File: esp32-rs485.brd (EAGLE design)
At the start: 160 x 100 mm, 24 parts, among them J1 GREEN-2P-3.5, U1 TEXAS_INSTRUMENTS_TPS54360DDA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, U2 MAX3485CSA

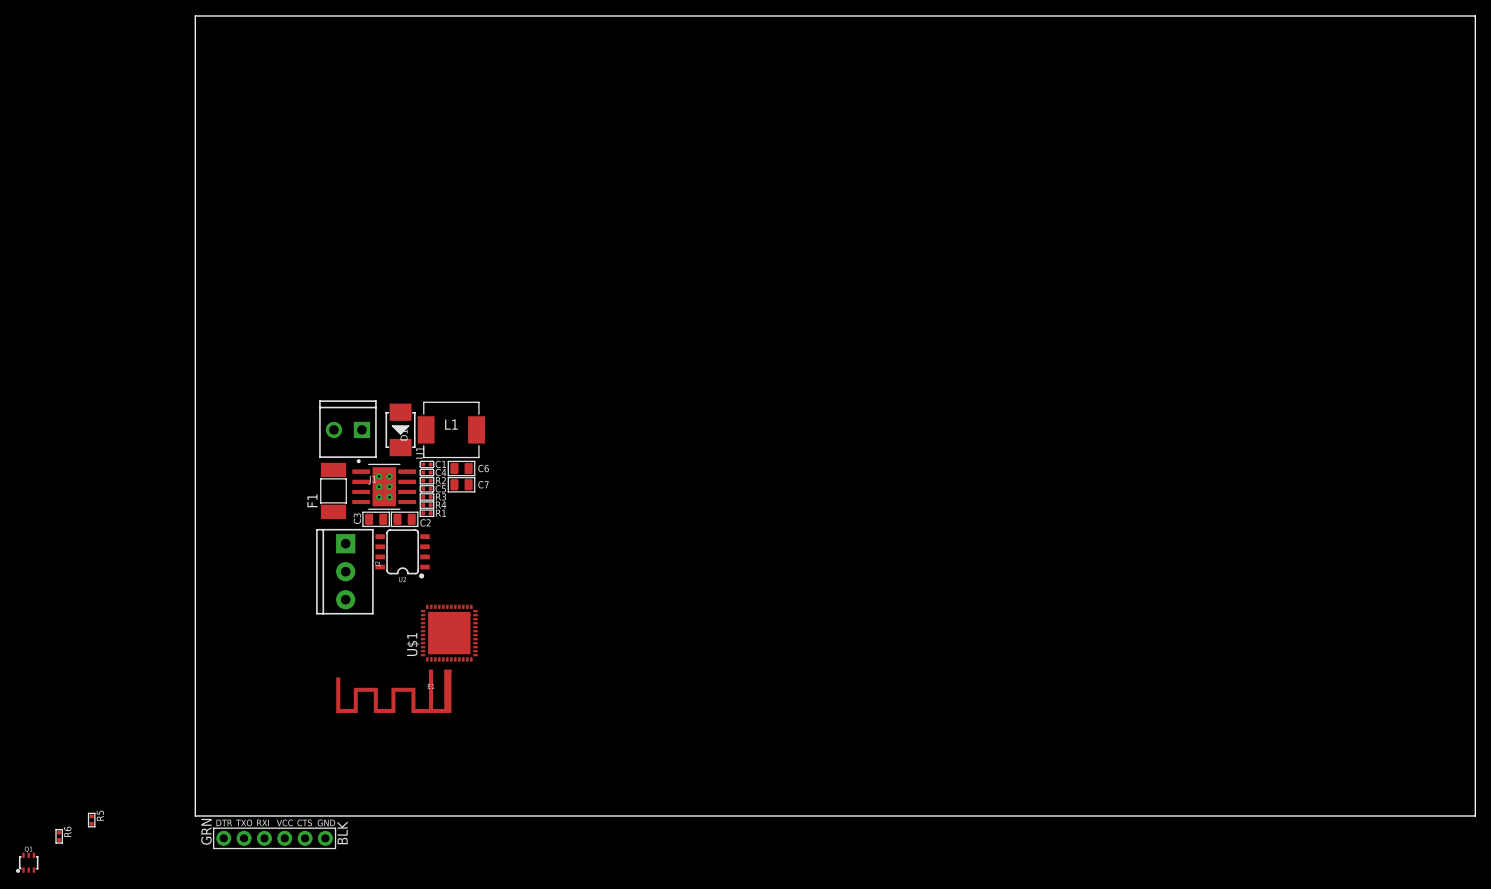
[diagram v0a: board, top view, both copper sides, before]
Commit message: Add MAX3485, CH340K and associated passives
Add MAX3485 TTL serial to RS-485 transceiver and associated passives.
Add CH340K USB to TTL serial chip and associated passives, ESP reset circuitry and PCB edge USB-C connector (must use 0.8mm PCB).
Complete PCB layout.
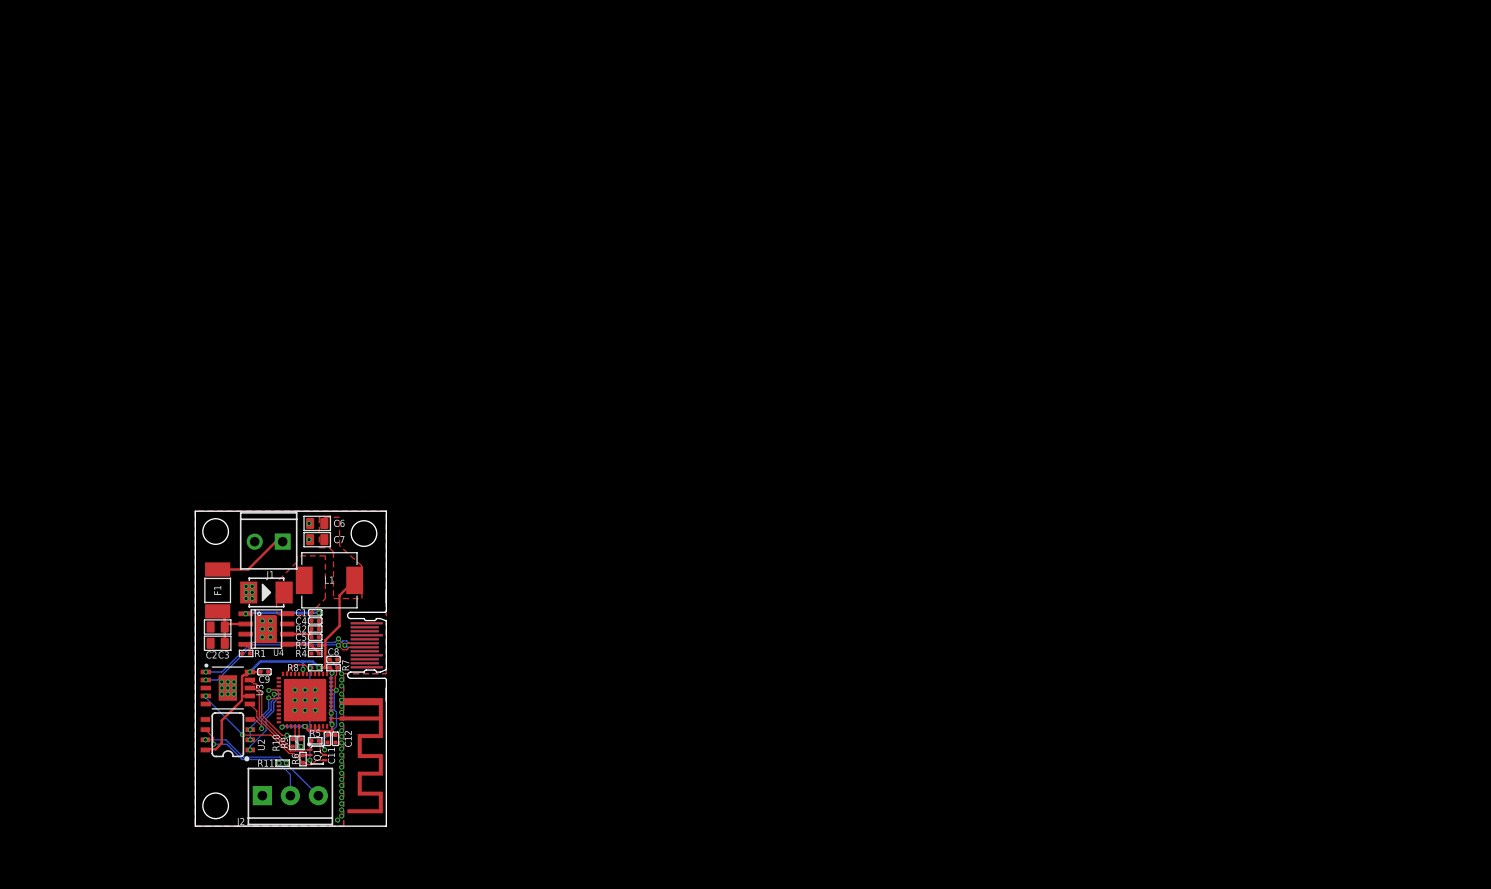
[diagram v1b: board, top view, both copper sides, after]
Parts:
- removed J3: (no value), SparkFun-Connectors:6_PIN_SERIAL_TARGET_SIDE_W_SILK
- removed U$1: ESP32-PICO-D4, ESP32-PICO-D4:QFN48
- added C11, C8, C9: 100nf, OPL_Capacitor:C0402
- added C12: 1UF 6.3V, OPL_Capacitor:C0402
- added R10, R9: 470R, OPL_Resistor:R0402
- added R11: 220R, OPL_Resistor:R0402
- added R7, R8: 10K 1/16W, OPL_Resistor:R0402
- added U$2: PCB_USB_C_2.0DS_2, USB_pcb_connectors:USB_TYPE_C_DS_2
- added U3: CH340K, CH340K:SOP100P600X180-11T230X320N
- added U4: TPS54360, we-power:SO08-PAD
- U1: value TEXAS_INSTRUMENTS_TPS54360DDARTEXAS_INSTRUMENTS_TPS54360DDAR_0_0 -> ESP32-PICO-D4; device Texas Instruments - TPS54360DDAR:TEXAS_INSTRUMENTS_TPS54360DDAR_0 -> ESP32-PICO-D4:QFN48
- moved Q1 38.5 mm to (15.2, 7.62), turned to 270 degrees
- moved J2 33.2 mm to (8.38, 2.54), turned to 0 degrees
- moved R6 32.0 mm to (13.5, 7.11), turned to 180 degrees
- moved U2 31.6 mm to (4.06, 10.2)
- moved R5 29.6 mm to (15.0, 9.40), turned to 90 degrees
- moved R1 28.6 mm to (6.35, 20.3), turned to 90 degrees
- moved U1 28.5 mm to (13.7, 14.5), turned to 180 degrees
- moved C2 27.0 mm to (2.79, 23.6), turned to 90 degrees
- moved D1 26.3 mm to (8.89, 27.9), turned to 0 degrees
- moved C3 25.2 mm to (2.79, 21.6)
- moved L1 24.2 mm to (16.8, 29.5)
- moved C1 23.2 mm to (15.0, 25.4)
- moved C4 23.2 mm to (15.0, 24.4)
- moved R3 23.2 mm to (15.0, 21.3)
- moved R4 23.2 mm to (15.0, 20.3), turned to 90 degrees
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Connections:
- removed net N$5: C2.2, C3.2, F1.1, U1.2
- removed net N$7: C5.2, R2.2, U1.6
- removed net VDD3P3_CPU: U$1.37
- removed net VDD3P3_RTC: U$1.19
- removed net VDDA_2: U$1.43
- removed net VDDA_3: U$1.46
- new net +24V: C2.2, C3.2, F1.1, U4.2
- new net DTR: Q1.4, R6.1, U3.4
- new net EN: C8.1, Q1.6, R7.1, U1.9
- new net GPIO0: Q1.3, R8.1, U1.23
- new net N$10: R10.1, U3.8
- new net N$11: R9.1, U3.9
- new net N$12: U$2.A6, U$2.B6, U3.2
- new net N$13: U$2.A7, U$2.B7, U3.1
- new net N$14: C5.2, R2.2, U4.6
- new net N$3: Q1.5, R5.2
- new net N$9: Q1.2, R6.2
- new net RTS: Q1.1, R5.1, U3.6
- new net U0RXD: R10.2, U1.40
- new net U0TXD: R9.2, U1.41
- net 3V3: now also C11.2, C12.2, C9.1, R7.2, R8.2, U1.1, U1.19, U1.3, U1.37, U1.4, U1.42, U1.43, U1.45, U1.46, U3.10, U3.7; no longer U$1.1, U$1.3, U$1.4
- net A: now also R11.1
- net B: now also R11.2
- net FB: now also U4.5; no longer U1.5
- net GND: now also C11.1, C12.1, C8.2, C9.2, U$2.A4, U$2.A9, U$2.B4, U$2.B9, U1.EXP, U3.11, U3.3, U4.7, U4.TP; no longer J3.P$6, U$1.EXP, U1.7, U1.9
- net N$1: now also U1.2; no longer U$1.2
- net N$2: now also U4.1; no longer U1.1
- net N$6: now also U4.4; no longer U1.4
- net SW: now also U4.8; no longer U1.8
- net U1RTS: now also U1.30; no longer U$1.30
- net U1RXD: now also U1.28; no longer U$1.28
- net U1TXD: now also U1.29; no longer U$1.29
- net VDD_SDIO_NC: now also U1.26; no longer U$1.26
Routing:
- net 3V3: track 0.00 -> 59.8 mm, vias 0 -> 8
- net N$12: track 0.00 -> 25.7 mm, vias 0 -> 2
- net N$13: track 0.00 -> 24.6 mm, vias 0 -> 3
- net DTR: track 0.00 -> 18.8 mm, vias 0 -> 2
- net B: track 0.00 -> 17.1 mm, vias 0 -> 2
- net A: track 0.00 -> 16.1 mm, vias 0 -> 2
- net GPIO0: track 0.00 -> 15.6 mm, vias 0 -> 2
- net EN: track 0.00 -> 13.3 mm, vias 0 -> 2
- net RTS: track 0.00 -> 11.7 mm
- net N$11: track 0.00 -> 11.7 mm, vias 0 -> 2
- net U1RXD: track 0.00 -> 11.4 mm, vias 0 -> 2
- net N$10: track 0.00 -> 10.1 mm
- net N$4: track 0.00 -> 9.57 mm
- net N$2: track 0.00 -> 9.21 mm, vias 0 -> 2
- net U1TXD: track 0.00 -> 7.64 mm, vias 0 -> 2
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- added copper zone on layer 1, net 3V3
- added copper zone on layer 1, net GND
- added copper zone on layer 16, net GND
- added copper zone on layer 1, net SW
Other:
- board size 160 x 100 mm -> 23.9 x 39.4 mm
- board text added: "USB 2.0 Type C"
